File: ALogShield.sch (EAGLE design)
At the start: 36 parts, among them IC1 LTC4412, J1 POWER_JACKPTH, Q1 FDN360P, Q2 FDN360P

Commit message: Transitioning to 2.0 update
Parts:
- removed CLOCK_BATT: 3V Backup Battery, SparkFun:BATTERY12PTH
- removed COUT: 1uF, SmartPrj:C-EUC0603
- removed C_LDO_SD, C_LDO_SENSE: >=2.2uF, resistor:C-EUC0603
- removed DECOUP: >=1uF, resistor:C-EUC0603
- removed H0: (no value), SparkFun:M083.5MM-8
- removed IC1: LTC4412, awickert:LTC4412ES6
- removed ISP: AVRISP-6, adafruit:AVRISP-6
- removed LD0_SD, LD0_SENSE: LP2985, adafruit:LP298XS
- removed LED: (no value), SparkFun:LED3MM
- removed LOGO1: OSHW-LOGOM, SparkFun-Aesthetics:OSHW-LOGOM
- removed LSHIFT: 4050D, 40xx:4050D
- removed MANUAL_LOG: Log Now, awickert:TL3350'TL3350'
- removed PU1, PU2: 4.7K, rcl:R-US_R0603
- removed Q1, Q2: FDN360P, transistor-power:FDN360P
- removed RSTAT: 470k, rcl:R-US_R0603
- removed RTC: DS3231SN, comfile:DS3231SN
- removed R_LED: 330, rcl:R-US_R0603
- removed R_REF_A0: Therm, resistor:R-US_0207/10
- removed R_REF_A1, R_REF_A2, R_REF_A3, R_REF_A6, R_REF_A7: (no value), resistor:R-US_0207/10
- removed S2: Reset, SparkFun:TAC_SWITCHSND
- removed SD: SDMMC06132, adafruit:SDMMC06132
- removed U$2: ALOG_LOGO_V1_5.5MM, awickert:ALOG_LOGO_V1_5.5MM
- removed U$3: NWLOGO_MED, awickert:NWLOGO_MED
- added 3V3: (no value), csandell:MIC5380
- added A0, A1, A2, A3: (no value), resistor:R-US_0207/10
- added C14: 10nF, rc-master-smd:CCA_ECJ-1206
- added CLOCK_BATT1: 3V Backup Battery, SparkFun:BATTERY12PTH
- added CLOCK_BATT_DECOUP, COUT1: 0.1uF, rcl:C-EUC0603
- added CLOCK_BATT_DECOUPLE: 10uF, SparkFun-Passives:CAP_POL1206
- added CLOCK_CIN1, CLOCK_CIN2, CLOCK_CIN3: 1uF, rcl:C-EUC0603
- added D1: BAT54C, semicon-smd-ipc:DIODE_AC-CA_
- added D2: BAT54, semicon-smd-ipc:DIODE_AC-CA_
- added H4, H5: (no value), SparkFun-Connectors:M10-3.5MM
- added ISP1: AVRISP-6, adafruit:AVRISP-6
- added LED1: (no value), SparkFun:LED3MM
- added LOG: LOG, SparkFun-Electromechanical:SWITCH-MOMENTARY-2PTH
- added LOGO2: OSHW-LOGOM, SparkFun-Aesthetics:OSHW-LOGOM
- added LSHIFT1: 4050D, 40xx:4050D
- added Q3, Q4: 2N7002PW, SparkFun-DiscreteSemi:MOSFET-NCHANNELSOT323
- added RCKL1, RCLK2: 220, rcl:R-US_R0603
- added RESET: Reset, SparkFun-Electromechanical:SWITCH-MOMENTARY-2PTH
- added RN2: 3.3K, resistor-dil:4R-N0603-ARC
- added R_LED1: 220, resistor:R-US_R0603
- added R_RESET: 10k, rcl:R-US_R0603
- added SD1: SDMMC06132, adafruit:SDMMC06132
- added U$1: ALOG_LOGO_V1_5.5MM, awickert:ALOG_LOGO_V1_5.5MM
- added U$4: NWLOGO, awickert:NWLOGO
- added U$5: NWLOGO_MED, awickert:NWLOGO_MED
- added U1: DS3231MZ/V+T, Maxim-DS3231MZ_8-SOIC:DS3231MZ/V+T
- H2: device SparkFun:M04SCREW -> SparkFun:M083.5MM-8
- J1: value POWER_JACKPTH -> (none); device SparkFun:POWER_JACKPTH -> SparkFun-Connectors:CONN_04SCREW
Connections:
- removed net A6: H2.1, R_REF_A6.2
- removed net A7: H2.3, R_REF_A7.2
- removed net BATTERY_POWER: IC1.VIN, Q1.D
- removed net CD_NOT_CONNECTED: SD.CARD_DETECT
- removed net D4-SENSE_3V3_SWITCH: LD0_SENSE.EN, U$9.D4
- removed net D8-SD_3V3_SWITCH: LD0_SD.EN, U$9.D8
- removed net LED+: LED.A, R_LED.2
- removed net N$7: IC1.STAT, Q2.G, RSTAT.1
- removed net N$8: IC1.GATE, Q1.G
- removed net VUSB: Q2.D
- new net 5V: H5.9
- new net CS-SD: LSHIFT1C.I
- new net D4-SENSE_LDO_SWITCH: 3V3.EN1, U$9.D4
- new net D6-CLOCK_SD_SWITCH: 3V3.EN2, U$9.D6
- new net D7-CS-EXT: H5.7, U$9.D7
- new net D8-EXT: H5.6, U$9.D8
- new net DTR: COUT1.1
- new net LED+1: LED1.A, R_LED1.2
- new net N$1: D1.A1, RCLK2.1
- new net N$11: D2.K, LOG.2
- new net N$2: CLOCK_BATT1.+, RCLK2.2
- new net N$67: D1.A2, RCKL1.1
- new net SCL_3V3: Q4.S, RN2C.1, U1.SCL
- new net SDA_3V3: Q3.S, RN2D.1, U1.SDA
- net +3V3: now also 3V3.VOUT1, CLOCK_CIN2.1, H2.6, H2.8, H5.8; no longer C_LDO_SENSE.2, H0.2, H0.4, H0.6, H0.8, LD0_SENSE.VOUT
- net A0: now also A0.2, C14C.1, H2.1; no longer H0.1, R_REF_A0.2
- net A1: now also A1.2, C14D.1, H2.3; no longer H0.3, R_REF_A1.2
- net A2: now also A2.2, C14A.1, H2.5; no longer H0.5, R_REF_A2.2
- net A3: now also A3.2, C14B.1, H2.7; no longer H0.7, R_REF_A3.2
- net BAT: now also CLOCK_BATT_DECOUP.1, CLOCK_BATT_DECOUPLE.+, D1.K, U1.VBAT; no longer CLOCK_BATT.+, RTC.VBAT
- net CLK: now also H5.4, ISP1.SCK, LSHIFT1A.I; no longer ISP.SCK, LSHIFTA.I
- net CS: no longer LSHIFTC.I
- net D3-INT1: now also H4.3
- net D5_MANUAL_LOG: now also D2.A2; no longer MANUAL_LOG.M1
- net D6: no longer U$9.D6
- net D7: no longer U$9.D7
- net D9-LED: now also R_LED1.1; no longer R_LED.1
- net DI: now also H5.2, ISP1.MOSI, LSHIFT1B.I; no longer ISP.MOSI, LSHIFTB.I
- net DO: now also H5.3, ISP1.MISO, SD1.DATA_OUT; no longer ISP.MISO, SD.DATA_OUT
- net GND: now also 3V3.GND, A0.1, A1.1, A2.1, A3.1, C14A.2, C14B.2, C14C.2, C14D.2, CLOCK_BATT1.-, CLOCK_BATT_DECOUP.2, CLOCK_BATT_DECOUPLE.-, CLOCK_CIN1.2, CLOCK_CIN2.2, CLOCK_CIN3.2, H4.6, H5.1, H5.10, ISP1.GND, J1.2, LED1.C, LOG.1, LSHIFT1D.I, LSHIFT1E.I, LSHIFT1F.I, LSHIFT1P.VSS, RESET.1, SD1.COMMON_SW, SD1.GND, SD1.VSS1, SD1.VSS2, U1.GND; no longer CLOCK_BATT.-, COUT.2, C_LDO_SD.1, C_LDO_SENSE.1, DECOUP.2, IC1.CTL, IC1.GND, ISP.GND, J1.GND, J1.GNDBREAK, LD0_SD.GND, LD0_SENSE.GND, LED.C, LSHIFTD.I, LSHIFTE.I, LSHIFTF.I, LSHIFTP.VSS, MANUAL_LOG.COM1, MANUAL_LOG.COM2, RTC.GND, RTC.NC1, RTC.NC2, RTC.NC3, RTC.NC4, RTC.NC5, RTC.NC6, RTC.NC7, RTC.NC8, R_REF_A0.1, R_REF_A1.1, R_REF_A2.1, R_REF_A3.1, R_REF_A6.1, R_REF_A7.1, S2.1, S2.2, SD.COMMON_SW, SD.GND, SD.VSS1, SD.VSS2
- net INT0: now also D2.A1, U1.*INT/SQW; no longer MANUAL_LOG.M2, RTC.!INT/SQW
- net RESET: now also COUT1.2, ISP1.RST, RESET.2, R_RESET.1; no longer ISP.RST, S2.3, S2.4
- net RX-I: now also H4.7
- net SCL: now also H4.10, Q4.D, RN2B.2; no longer PU1.1, RTC.SCL
- net SDA: now also H4.9, Q3.D, RN2A.2; no longer PU2.1, RTC.SDA
- net SD_CLK: now also LSHIFT1A.O, SD1.SCLK; no longer LSHIFTA.O, SD.SCLK
- net SD_CS: now also LSHIFT1C.O, SD1.CS; no longer LSHIFTC.O, SD.CS
- net SD_DI: now also LSHIFT1B.O, SD1.DATA_IN; no longer LSHIFTB.O, SD.DATA_IN
- net TX-O: now also H4.8
- net VCC: now also 3V3.VIN, CLOCK_CIN1.1, H4.5, H5.5, ISP1.VCC, J1.1, RCKL1.2, RN2A.1, RN2B.1, R_RESET.2; no longer COUT.1, DECOUP.1, IC1.SEN, ISP.VCC, J1.PWR, LD0_SD.VIN, LD0_SENSE.VIN, PU1.2, PU2.2, Q1.S, Q2.S, RSTAT.2, RTC.VCC
- net VDD: now also 3V3.VOUT2, CLOCK_CIN3.1, LSHIFT1P.VDD, Q3.G, Q4.G, RN2C.2, RN2D.2, SD1.VDD, U1.VCC; no longer C_LDO_SD.2, LD0_SD.VOUT, LSHIFTP.VDD, SD.VDD
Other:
- note added: "1/4"
- note added: "2.0"
- note added: "2/4"
- note added: "3/4"
- note added: "4/4"
- note added: "ALOG"
- note added: "MICROCONTROLLER"
- note added: "POWER MANAGEMENT & DECOUPLING"
- note added: "REAL TIME CLOCK"
- note added: "SD CARD AND LEVEL SHIFTER"
- note added: "USER IO & REFERENCE RESISTORS"
- note removed: "3V3 = Sensor 3V3"
- note removed: "Make sure that just this single 1uF cap can handle 2 LDO regulators"
- note removed: "VDD = SD3V3"

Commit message: Semi-final parts; not placed or labeled properly
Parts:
- removed D1: BAT54C, semicon-smd-ipc:DIODE_AC-CA_
- removed H1: (no value), SparkFun:M083.5MM-8
- removed H5: (no value), SparkFun-Connectors:M10-3.5MM
- removed Q3, Q4: 2N7002PW, SparkFun-DiscreteSemi:MOSFET-NCHANNELSOT323
- removed RCKL1, RCLK2: 220, rcl:R-US_R0603
- added J2: (no value), SparkFun-Connectors:CONN_04SCREW
- H4: device SparkFun-Connectors:M10-3.5MM -> SparkFun:M083.5MM-8
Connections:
- removed net 5V: H5.9
- removed net D6: H1.5
- removed net D7: H1.6
- removed net N$1: D1.A1, RCLK2.1
- removed net N$2: CLOCK_BATT1.+, RCLK2.2
- removed net N$67: D1.A2, RCKL1.1
- removed net SCL_3V3: Q4.S, RN2C.1, U1.SCL
- removed net SDA_3V3: Q3.S, RN2D.1, U1.SDA
- net +3V3: now also H4.8; no longer H5.8
- net BAT: now also CLOCK_BATT1.+; no longer D1.K
- net CLK: now also H4.4; no longer H5.4
- net D3-INT1: now also J2.2; no longer H1.1, H4.3
- net D7-CS-EXT: now also H4.7; no longer H5.7
- net D8-EXT: now also H4.6; no longer H5.6
- net DI: now also H4.2; no longer H5.2
- net DO: now also H4.3; no longer H5.3
- net GND: now also H4.1, J2.1; no longer H1.2, H1.4, H1.7, H4.6, H5.1, H5.10
- net RX-I: now also J2.3; no longer H3.1, H4.7
- net SCL: now also J1.4, RN2C.1, U1.SCL; no longer H4.10, Q4.D, RN2B.2
- net SDA: now also J1.3, RN2D.1, U1.SDA; no longer H4.9, Q3.D, RN2A.2
- net TX-O: now also J2.4; no longer H3.2, H4.8
- net VCC: now also RN2C.2, RN2D.2, U1.VCC; no longer H1.3, H1.8, H5.5, RCKL1.2, RN2A.1, RN2B.1
- net VDD: no longer Q3.G, Q4.G, RN2C.2, RN2D.2, U1.VCC
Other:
- moved on the sheet: CLOCK_BATT1, H2, J1

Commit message: Components placed
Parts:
- removed RN2: 3.3K, resistor-dil:4R-N0603-ARC
- removed U$5: NWLOGO_MED, awickert:NWLOGO_MED
- added SCL_PU, SDA_PU: 10k, rcl:R-US_R0603
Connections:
- net A0: now also C14D.1; no longer C14C.1
- net A1: now also C14C.1; no longer C14D.1
- net A2: now also C14B.1; no longer C14A.1
- net A3: now also C14A.1; no longer C14B.1
- net CLK: now also H4.2; no longer H4.4
- net DI: now also H4.4; no longer H4.2
- net SCL: now also SCL_PU.1; no longer RN2C.1
- net SDA: now also SDA_PU.1; no longer RN2D.1
- net VCC: now also SCL_PU.2, SDA_PU.2; no longer RN2C.2, RN2D.2
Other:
- moved on the sheet: C14A, C14B, C14C, C14D
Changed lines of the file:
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@@
 <?xml version="1.0" encoding="utf-8"?>
 <!DOCTYPE eagle SYSTEM "eagle.dtd">
-<eagle version="6.6.0">
+<eagle version="7.7.0">
 <drawing>
 <settings>
@@
 <part name="CLOCK_BATT_DECOUP" library="rcl" deviceset="C-EU" device="C0603" value="0.1uF"/>
 <part name="SUPPLY56" library="supply2" deviceset="GND" device=""/>
-<part name="U$5" library="awickert" deviceset="NWLOGO_MED" device=""/>
 <part name="COUT1" library="rcl" deviceset="C-EU" device="C0603" value="0.1uF"/>
 <part name="D2" library="semicon-smd-ipc" deviceset="DIODE_AC-CA_" device="" value="BAT54"/>
 <part name="LOG" library="SparkFun-Electromechanical" deviceset="SWITCH-MOMENTARY-2" device="PTH" value="LOG"/>
-<part name="RN2" library="resistor-dil" deviceset="4R-N" device="0603-ARC" value="3.3K"/>
 <part name="CLOCK_BATT_DECOUPLE" library="SparkFun-Passives" deviceset="CAP_POL" device="1206" value="10uF"/>
 <part name="U1" library="Maxim-DS3231MZ_8-SOIC" deviceset="DS3231MZ/V+T" device=""/>
@@
 <part name="SUPPLY3" library="supply2" deviceset="GND" device=""/>
 <part name="J2" library="SparkFun-Connectors" deviceset="CONN_04" device="SCREW"/>
+<part name="SCL_PU" library="rcl" deviceset="R-US_" device="R0603" value="10k"/>
+<part name="SDA_PU" library="rcl" deviceset="R-US_" device="R0603" value="10k"/>
 </parts>
 <sheets>
@@
 <instance part="SUPPLY52" gate="GND" x="109.22" y="-200.66"/>
 <instance part="RESET" gate="G$1" x="157.48" y="-182.88" rot="R90"/>
-<instance part="C14" gate="A" x="48.26" y="-185.42"/>
-<instance part="C14" gate="B" x="48.26" y="-195.58"/>
-<instance part="C14" gate="C" x="48.26" y="-165.1"/>
-<instance part="C14" gate="D" x="48.26" y="-175.26"/>
+<instance part="C14" gate="A" x="48.26" y="-195.58"/>
+<instance part="C14" gate="B" x="48.26" y="-185.42"/>
+<instance part="C14" gate="C" x="48.26" y="-175.26"/>
+<instance part="C14" gate="D" x="48.26" y="-165.1"/>
 <instance part="SUPPLY53" gate="GND" x="63.5" y="-208.28"/>
 <instance part="CLOCK_BATT_DECOUP" gate="G$1" x="99.06" y="-411.48" smashed="yes">
@@
 </instance>
 <instance part="SUPPLY56" gate="GND" x="137.16" y="-426.72"/>
-<instance part="U$5" gate="G$1" x="210.82" y="-469.9"/>
 <instance part="COUT1" gate="G$1" x="142.24" y="-175.26" rot="R90"/>
 <instance part="D2" gate="G$1" x="109.22" y="-160.02" rot="R180"/>
 <instance part="LOG" gate="G$1" x="109.22" y="-177.8" rot="R90"/>
-<instance part="RN2" gate="C" x="114.3" y="-398.78" smashed="yes" rot="R90">
-<attribute name="VALUE" x="112.268" y="-401.32" size="1.778" layer="96" rot="R90"/>
-<attribute name="NAME" x="117.348" y="-401.32" size="1.778" layer="95" rot="R90"/>
-</instance>
-<instance part="RN2" gate="D" x="124.46" y="-401.32" smashed="yes" rot="R90">
-<attribute name="VALUE" x="122.428" y="-401.32" size="1.778" layer="96" rot="R90"/>
-<attribute name="NAME" x="127.508" y="-403.86" size="1.778" layer="95" rot="R90"/>
-</instance>
 <instance part="CLOCK_BATT_DECOUPLE" gate="G$1" x="109.22" y="-411.48" smashed="yes">
 <attribute name="NAME" x="94.996" y="-426.085" size="1.778" layer="95"/>
@@
 <instance part="SUPPLY3" gate="GND" x="99.06" y="-134.62"/>
 <instance part="J2" gate="G$1" x="134.62" y="-134.62" rot="R180"/>
+<instance part="SCL_PU" gate="G$1" x="114.3" y="-398.78" rot="R90"/>
+<instance part="SDA_PU" gate="G$1" x="124.46" y="-401.32" rot="R90"/>
 </instances>
 <busses>
@@
 <segment>
 <wire x1="124.46" y1="-391.16" x2="124.46" y2="-396.24" width="0.1524" layer="91"/>
-<pinref part="RN2" gate="D" pin="2"/>
 <pinref part="P+5" gate="VCC" pin="VCC"/>
+<pinref part="SDA_PU" gate="G$1" pin="2"/>
 </segment>
 <segment>
 <wire x1="114.3" y1="-388.62" x2="114.3" y2="-393.7" width="0.1524" layer="91"/>
-<pinref part="RN2" gate="C" pin="2"/>
 <pinref part="P+7" gate="VCC" pin="VCC"/>
+<pinref part="SCL_PU" gate="G$1" pin="2"/>
 </segment>
 <segment>
@@
 </segment>
 <segment>
-<wire x1="129.54" y1="-114.3" x2="116.84" y2="-114.3" width="0.1524" layer="91"/>
-<label x="116.84" y="-114.3" size="1.778" layer="95"/>
-<pinref part="H4" gate="G$1" pin="2"/>
+<wire x1="129.54" y1="-119.38" x2="116.84" y2="-119.38" width="0.1524" layer="91"/>
+<label x="116.84" y="-119.38" size="1.778" layer="95"/>
+<pinref part="H4" gate="G$1" pin="4"/>
 </segment>
 </net>
@@
 </segment>
 <segment>
-<wire x1="129.54" y1="-119.38" x2="116.84" y2="-119.38" width="0.1524" layer="91"/>
-<label x="116.84" y="-119.38" size="1.778" layer="95"/>
-<pinref part="H4" gate="G$1" pin="4"/>
+<wire x1="129.54" y1="-114.3" x2="116.84" y2="-114.3" width="0.1524" layer="91"/>
+<label x="116.84" y="-114.3" size="1.778" layer="95"/>
+<pinref part="H4" gate="G$1" pin="2"/>
 </segment>
 </net>
@@
 <pinref part="SUPPLY53" gate="GND" pin="GND"/>
 <wire x1="63.5" y1="-165.1" x2="63.5" y2="-175.26" width="0.1524" layer="91"/>
-<pinref part="C14" gate="C" pin="2"/>
+<pinref part="C14" gate="D" pin="2"/>
 <wire x1="63.5" y1="-175.26" x2="63.5" y2="-185.42" width="0.1524" layer="91"/>
 <wire x1="63.5" y1="-185.42" x2="63.5" y2="-195.58" width="0.1524" layer="91"/>
 <wire x1="63.5" y1="-195.58" x2="63.5" y2="-205.74" width="0.1524" layer="91"/>
 <wire x1="50.8" y1="-165.1" x2="63.5" y2="-165.1" width="0.1524" layer="91"/>
-<pinref part="C14" gate="D" pin="2"/>
+<pinref part="C14" gate="C" pin="2"/>
 <wire x1="50.8" y1="-175.26" x2="63.5" y2="-175.26" width="0.1524" layer="91"/>
+<junction x="63.5" y="-175.26"/>
+<pinref part="C14" gate="B" pin="2"/>
 <wire x1="50.8" y1="-185.42" x2="63.5" y2="-185.42" width="0.1524" layer="91"/>
+<junction x="63.5" y="-185.42"/>
+<pinref part="C14" gate="A" pin="2"/>
 <wire x1="50.8" y1="-195.58" x2="63.5" y2="-195.58" width="0.1524" layer="91"/>
-<junction x="63.5" y="-165.1"/>
-<junction x="63.5" y="-175.26"/>
-<junction x="63.5" y="-185.42"/>
 <junction x="63.5" y="-195.58"/>
-<pinref part="C14" gate="A" pin="2"/>
-<pinref part="C14" gate="B" pin="2"/>
 </segment>
 <segment>
@@
 </segment>
 <segment>
+<pinref part="C14" gate="B" pin="1"/>
 <pinref part="A2" gate="G$1" pin="2"/>
-<label x="38.1" y="-185.42" size="1.778" layer="95"/>
-<wire x1="35.56" y1="-185.42" x2="45.72" y2="-185.42" width="0.1524" layer="91"/>
-<pinref part="C14" gate="A" pin="1"/>
+<wire x1="45.72" y1="-185.42" x2="35.56" y2="-185.42" width="0.1524" layer="91"/>
 </segment>
 </net>
@@
 <wire x1="91.44" y1="-403.86" x2="114.3" y2="-403.86" width="0.1524" layer="91"/>
 <label x="99.06" y="-403.86" size="1.778" layer="95"/>
-<pinref part="RN2" gate="C" pin="1"/>
 <pinref part="U1" gate="A" pin="SCL"/>
+<pinref part="SCL_PU" gate="G$1" pin="1"/>
 </segment>
 </net>
@@
 <wire x1="91.44" y1="-406.4" x2="124.46" y2="-406.4" width="0.1524" layer="91"/>
 <label x="99.06" y="-406.4" size="1.778" layer="95"/>
-<pinref part="RN2" gate="D" pin="1"/>
 <pinref part="U1" gate="A" pin="SDA"/>
+<pinref part="SDA_PU" gate="G$1" pin="1"/>
 </segment>
 </net>
@@
 <segment>
 <pinref part="A0" gate="G$1" pin="2"/>
-<pinref part="C14" gate="C" pin="1"/>
-<label x="38.1" y="-165.1" size="1.778" layer="95"/>
+<pinref part="C14" gate="D" pin="1"/>
 <wire x1="35.56" y1="-165.1" x2="45.72" y2="-165.1" width="0.1524" layer="91"/>
 </segment>
@@
 <segment>
 <pinref part="A3" gate="G$1" pin="2"/>
-<label x="38.1" y="-195.58" size="1.778" layer="95"/>
+<pinref part="C14" gate="A" pin="1"/>
 <wire x1="35.56" y1="-195.58" x2="45.72" y2="-195.58" width="0.1524" layer="91"/>
-<pinref part="C14" gate="B" pin="1"/>
 </segment>
 </net>
@@
 <segment>
 <pinref part="A1" gate="G$1" pin="2"/>
-<pinref part="C14" gate="D" pin="1"/>
-<label x="38.1" y="-175.26" size="1.778" layer="95"/>
+<pinref part="C14" gate="C" pin="1"/>
 <wire x1="35.56" y1="-175.26" x2="45.72" y2="-175.26" width="0.1524" layer="91"/>
 </segment>

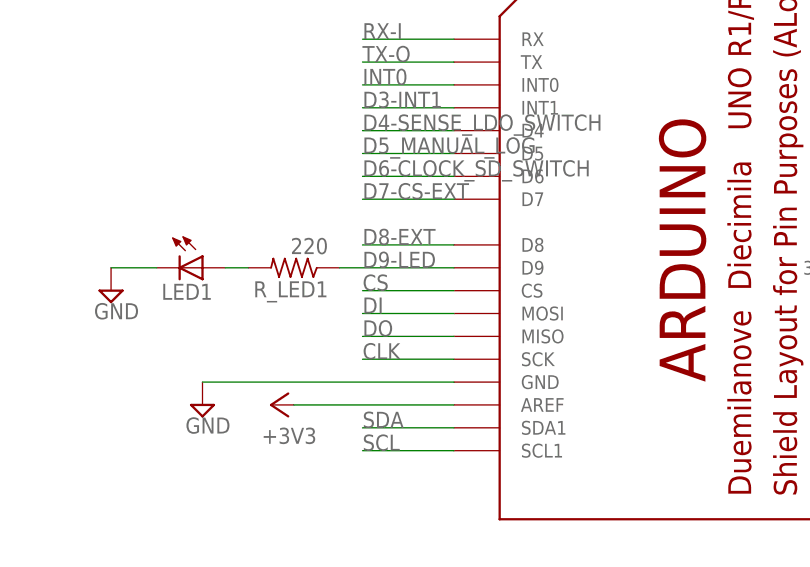
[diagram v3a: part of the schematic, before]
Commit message: Connect CS and CS-SD: rename to CS-SD
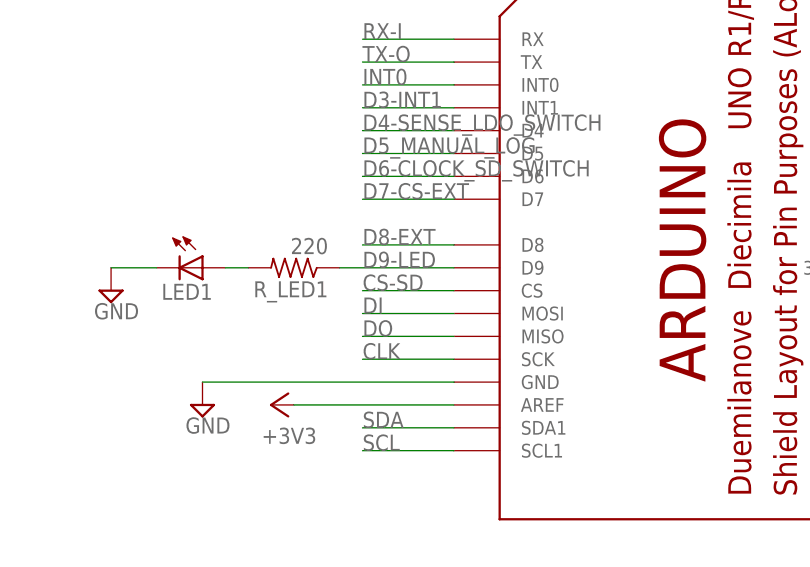
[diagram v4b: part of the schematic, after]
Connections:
- removed net CS: U$9.CS
- net CS-SD: now also U$9.CS
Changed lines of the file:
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@@
-</segment>
-</net>
-<net name="CS" class="0">
-<segment>
-<wire x1="53.34" y1="-63.5" x2="63.5" y2="-63.5" width="0.1524" layer="91"/>
-<pinref part="U$9" gate="G$1" pin="CS"/>
-<label x="53.34" y="-63.5" size="1.778" layer="95"/>
 </segment>
 </net>
@@
 <pinref part="LSHIFT1" gate="C" pin="I"/>
 </segment>
-</net>
+<segment>
+<wire x1="53.34" y1="-63.5" x2="63.5" y2="-63.5" width="0.1524" layer="91"/>
+<pinref part="U$9" gate="G$1" pin="CS"/>
+<label x="53.34" y="-63.5" size="1.778" layer="95"/>
+</segment>
+</net>

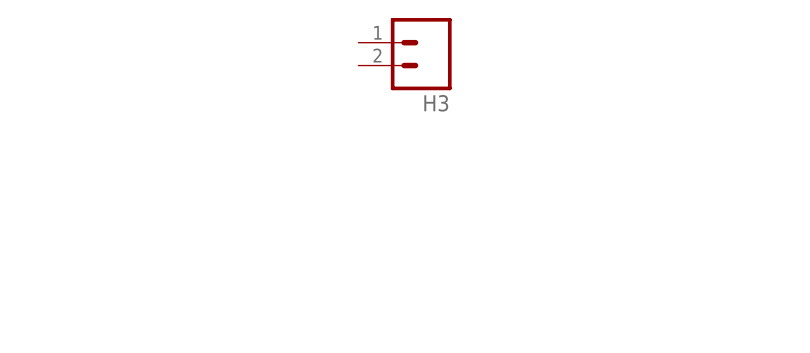
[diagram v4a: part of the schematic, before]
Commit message: Remove JST power connector; move buttons to symmetrical places
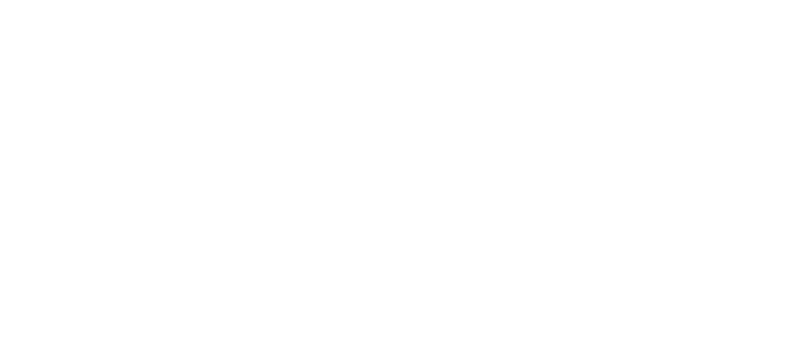
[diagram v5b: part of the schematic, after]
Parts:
- removed H3: (no value), SparkFun-Connectors:M023.5MM
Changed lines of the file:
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@@
 <part name="SUPPLY40" library="supply2" deviceset="GND" device=""/>
 <part name="+3V5" library="supply1" deviceset="+3V3" device=""/>
-<part name="H3" library="SparkFun-Connectors" deviceset="M02" device="3.5MM"/>
 <part name="LSHIFT1" library="40xx" deviceset="4050" device="D"/>
 <part name="SUPPLY7" library="supply2" deviceset="GND" device=""/>
@@
 <instance part="SUPPLY40" gate="GND" x="134.62" y="-71.12"/>
 <instance part="+3V5" gate="G$1" x="152.4" y="-60.96"/>
-<instance part="H3" gate="G$1" x="299.72" y="99.06" rot="R180"/>
 <instance part="LSHIFT1" gate="A" x="231.14" y="-289.56"/>
 <instance part="LSHIFT1" gate="B" x="231.14" y="-279.4"/>
